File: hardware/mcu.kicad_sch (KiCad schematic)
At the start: 36 parts, among them U1 74LVC125, U2 STM32F407VETx, U3 24LC64, U7 74LVC125, X1 12MHz

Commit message: Update PrntrBoard fabrication files.
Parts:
- X1: Part # (none) -> SIT1602AI-22-33E-12.000000D; Part# SIT1602AI-22-33E-12.000000D -> (none)

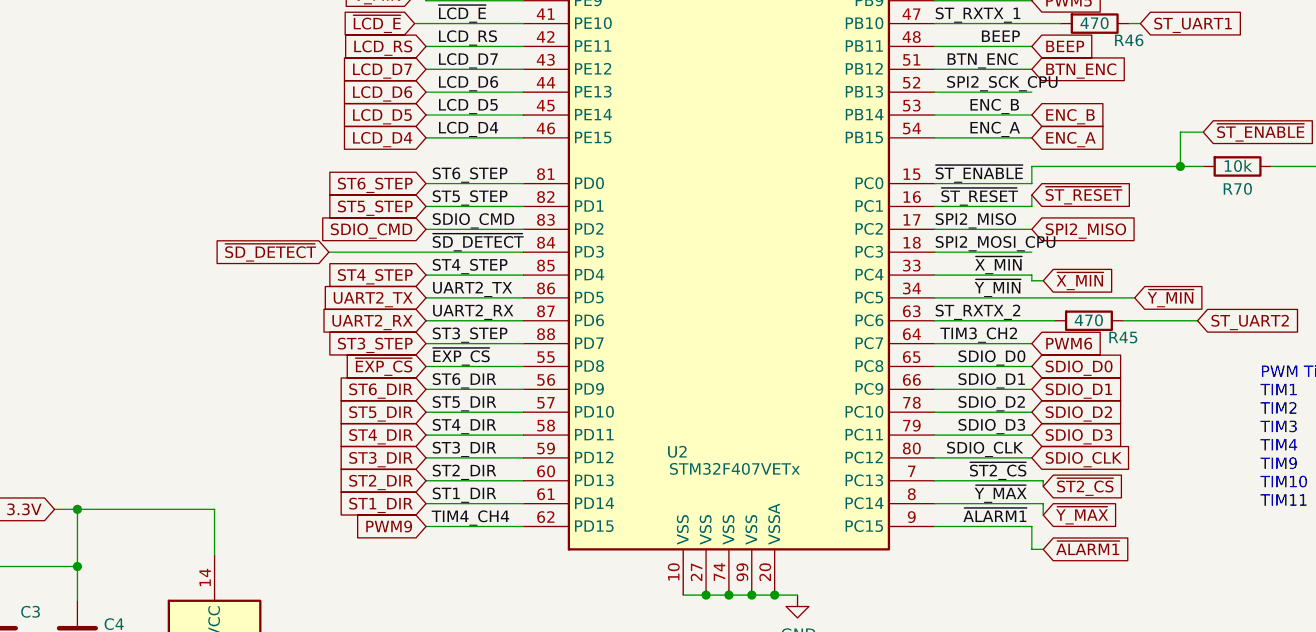
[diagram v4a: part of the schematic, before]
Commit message: Added CAN
- Added CAN interface (PD0-1) with RJ 6p6c terminal
- SD card moved to back /left side and switched to SPI mode
- removed  EXP4 headrr
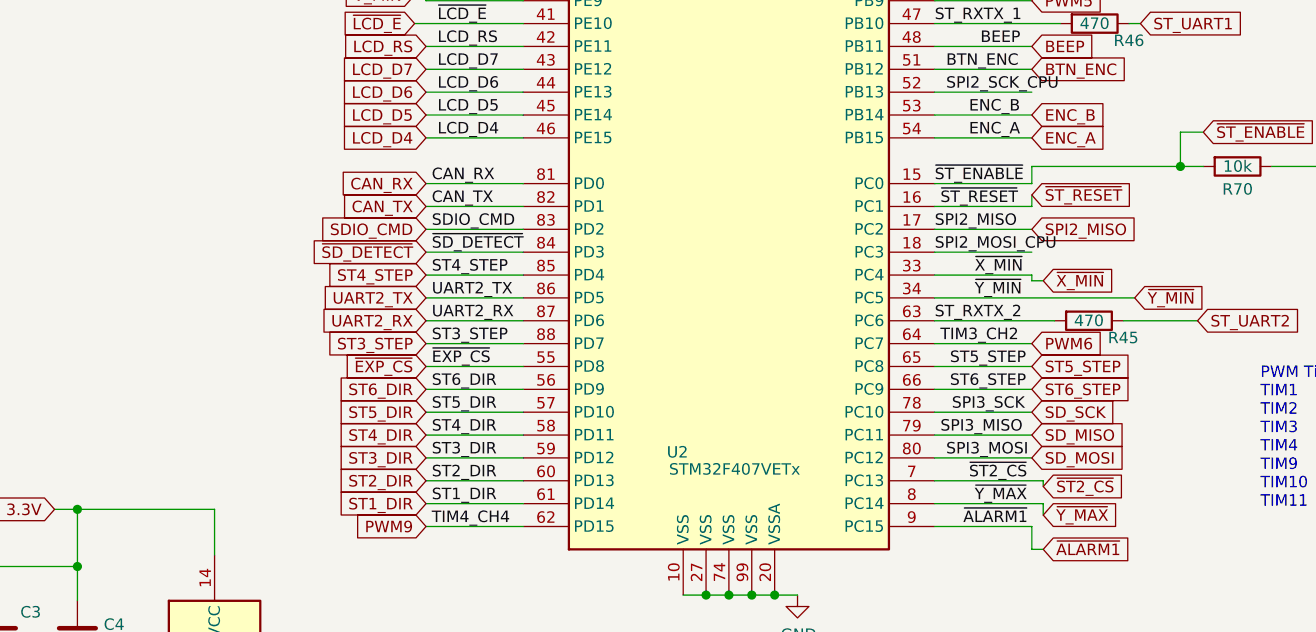
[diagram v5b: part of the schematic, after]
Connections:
- net SDIO_D0 is gone; now on net ST5_STEP: U2.65 (PC8)
- net SDIO_D1 is gone; now on net ST6_STEP: U2.66 (PC9)
- net ST5_STEP: no longer U2.82 (PD1)
- net ST6_STEP: no longer U2.81 (PD0)
- net SDIO_CLK renamed SD_MOSI
- net SDIO_D2 renamed SD_SCK
- net SDIO_D3 renamed SD_MISO
- new net CAN_RX: U2.81 (PD0)
- new net CAN_TX: U2.82 (PD1)
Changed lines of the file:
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@@
   (junction (at 269.24 155.575) (diameter 1.016) (color 0 0 0 0))
   (no_connect (at 262.255 53.975))
+  (no_connect (at 262.255 75.565))
+  (no_connect (at 262.255 64.77))
   (no_connect (at 211.455 89.535))
   (no_connect (at 80.645 69.85))
-  (no_connect (at 262.255 64.77))
-  (no_connect (at 262.255 75.565))
   (wire (pts (xy 22.225 160.655) (xy 31.115 160.655))
     (stroke (width 0) (type solid) (color 0 0 0 0))
@@
     (stroke (width 0) (type solid) (color 0 0 0 0))
   )
-  (wire (pts (xy 59.055 125.73) (xy 80.645 125.73))
-    (stroke (width 0) (type solid) (color 0 0 0 0))
-  )
   (wire (pts (xy 59.69 85.09) (xy 80.645 85.09))
     (stroke (width 0) (type solid) (color 0 0 0 0))
@@
     (stroke (width 0) (type solid) (color 0 0 0 0))
   )
+  (wire (pts (xy 69.85 125.73) (xy 80.645 125.73))
+    (stroke (width 0) (type solid) (color 0 0 0 0))
+  )
   (wire (pts (xy 70.485 177.8) (xy 86.995 177.8))
     (stroke (width 0) (type solid) (color 0 0 0 0))
@@
     (effects (font (size 1.27 1.27)) (justify left bottom))
   )
-  (label "ST6_STEP" (at 70.485 118.11 0)
-    (effects (font (size 1.27 1.27)) (justify left bottom))
-  )
-  (label "ST5_STEP" (at 70.485 120.65 0)
+  (label "CAN_RX" (at 70.485 118.11 0)
+    (effects (font (size 1.27 1.27)) (justify left bottom))
+  )
+  (label "CAN_TX" (at 70.485 120.65 0)
     (effects (font (size 1.27 1.27)) (justify left bottom))
   )
@@
     (effects (font (size 1.27 1.27)) (justify left bottom))
   )
+  (label "SPI3_MISO" (at 127 146.05 0)
+    (effects (font (size 1.27 1.27)) (justify left bottom))
+  )
   (label "SPI2_MOSI_CPU" (at 127 174.625 0)
     (effects (font (size 1.27 1.27)) (justify left bottom))
@@
     (effects (font (size 1.27 1.27)) (justify left bottom))
   )
-  (label "SDIO_CLK" (at 127.635 148.59 0)
+  (label "SPI3_MOSI" (at 127.635 148.59 0)
     (effects (font (size 1.27 1.27)) (justify left bottom))
   )
@@
     (effects (font (size 1.27 1.27)) (justify left bottom))
   )
+  (label "SPI3_SCK" (at 128.27 143.51 0)
+    (effects (font (size 1.27 1.27)) (justify left bottom))
+  )
   (label "USB_D-" (at 128.905 59.69 0)
     (effects (font (size 1.27 1.27)) (justify left bottom))
@@
     (effects (font (size 1.27 1.27)) (justify left bottom))
   )
-  (label "SDIO_D0" (at 128.905 138.43 0)
-    (effects (font (size 1.27 1.27)) (justify left bottom))
-  )
-  (label "SDIO_D1" (at 128.905 140.97 0)
-    (effects (font (size 1.27 1.27)) (justify left bottom))
-  )
-  (label "SDIO_D2" (at 128.905 143.51 0)
-    (effects (font (size 1.27 1.27)) (justify left bottom))
-  )
-  (label "SDIO_D3" (at 128.905 146.05 0)
-    (effects (font (size 1.27 1.27)) (justify left bottom))
-  )
   (label "~ALARM1" (at 129.54 156.21 0)
     (effects (font (size 1.27 1.27)) (justify left bottom))
@@
     (effects (font (size 1.27 1.27)) (justify left bottom))
   )
+  (label "ST5_STEP" (at 136.525 138.43 180)
+    (effects (font (size 1.27 1.27)) (justify right bottom))
+  )
+  (label "ST6_STEP" (at 136.525 140.97 180)
+    (effects (font (size 1.27 1.27)) (justify right bottom))
+  )
   (label "BOOT0" (at 190.5 78.105 0)
     (effects (font (size 1.27 1.27)) (justify left bottom))
@@
     (effects (font (size 1.27 1.27)) (justify right))
   )
-  (global_label "~SD_DETECT" (shape input) (at 59.055 125.73 180)    (property "Intersheet References" "${INTERSHEET_REFS}" (id 0) (at 0 0 0)
-      (effects (font (size 1.27 1.27)) hide)
-    )
-    (effects (font (size 1.27 1.27)) (justify right))
-  )
   (global_label "~ST3_CS" (shape input) (at 59.69 85.09 180)    (property "Intersheet References" "${INTERSHEET_REFS}" (id 0) (at 0 0 0)
       (effects (font (size 1.27 1.27)) hide)
@@
     (effects (font (size 1.27 1.27)) (justify right))
   )
-  (global_label "ST6_STEP" (shape input) (at 69.85 118.11 180)    (property "Intersheet References" "${INTERSHEET_REFS}" (id 0) (at 0 0 0)
-      (effects (font (size 1.27 1.27)) hide)
-    )
-    (effects (font (size 1.27 1.27)) (justify right))
-  )
-  (global_label "ST5_STEP" (shape input) (at 69.85 120.65 180)    (property "Intersheet References" "${INTERSHEET_REFS}" (id 0) (at 0 0 0)
-      (effects (font (size 1.27 1.27)) hide)
+  (global_label "CAN_RX" (shape input) (at 69.85 118.11 180)    (property "Intersheet References" "${INTERSHEET_REFS}" (id 0) (at 57.5067 120.5706 0)
+      (effects (font (size 1.27 1.27)) (justify right) hide)
+    )
+    (effects (font (size 1.27 1.27)) (justify right))
+  )
+  (global_label "CAN_TX" (shape input) (at 69.85 120.65 180)    (property "Intersheet References" "${INTERSHEET_REFS}" (id 0) (at 57.8091 118.0306 0)
+      (effects (font (size 1.27 1.27)) (justify right) hide)
     )
     (effects (font (size 1.27 1.27)) (justify right))
@@
     (effects (font (size 1.27 1.27)) (justify right))
   )
+  (global_label "~SD_DETECT" (shape input) (at 69.85 125.73 180)    (property "Intersheet References" "${INTERSHEET_REFS}" (id 0) (at 10.795 0 0)
+      (effects (font (size 1.27 1.27)) hide)
+    )
+    (effects (font (size 1.27 1.27)) (justify right))
+  )
   (global_label "ST4_STEP" (shape input) (at 69.85 128.27 180)    (property "Intersheet References" "${INTERSHEET_REFS}" (id 0) (at 0 0 0)
       (effects (font (size 1.27 1.27)) hide)
@@
     (effects (font (size 1.27 1.27)) (justify left))
   )
-  (global_label "SDIO_D0" (shape input) (at 137.16 138.43 0)    (property "Intersheet References" "${INTERSHEET_REFS}" (id 0) (at 0 0 0)
-      (effects (font (size 1.27 1.27)) hide)
-    )
-    (effects (font (size 1.27 1.27)) (justify left))
-  )
-  (global_label "SDIO_D1" (shape input) (at 137.16 140.97 0)    (property "Intersheet References" "${INTERSHEET_REFS}" (id 0) (at 0 0 0)
-      (effects (font (size 1.27 1.27)) hide)
-    )
-    (effects (font (size 1.27 1.27)) (justify left))
-  )
-  (global_label "SDIO_D2" (shape input) (at 137.16 143.51 0)    (property "Intersheet References" "${INTERSHEET_REFS}" (id 0) (at 0 0 0)
-      (effects (font (size 1.27 1.27)) hide)
-    )
-    (effects (font (size 1.27 1.27)) (justify left))
-  )
-  (global_label "SDIO_D3" (shape input) (at 137.16 146.05 0)    (property "Intersheet References" "${INTERSHEET_REFS}" (id 0) (at 0 0 0)
-      (effects (font (size 1.27 1.27)) hide)
-    )
-    (effects (font (size 1.27 1.27)) (justify left))
-  )
-  (global_label "SDIO_CLK" (shape input) (at 137.16 148.59 0)    (property "Intersheet References" "${INTERSHEET_REFS}" (id 0) (at 0 0 0)
-      (effects (font (size 1.27 1.27)) hide)
-    )
-    (effects (font (size 1.27 1.27)) (justify left))
+  (global_label "ST5_STEP" (shape input) (at 137.16 138.43 0)    (property "Intersheet References" "${INTERSHEET_REFS}" (id 0) (at 207.01 259.08 0)
+      (effects (font (size 1.27 1.27)) hide)
+    )
+    (effects (font (size 1.27 1.27)) (justify left))
+  )
+  (global_label "ST6_STEP" (shape input) (at 137.16 140.97 0)    (property "Intersheet References" "${INTERSHEET_REFS}" (id 0) (at 207.01 259.08 0)
+      (effects (font (size 1.27 1.27)) hide)
+    )
+    (effects (font (size 1.27 1.27)) (justify left))
+  )
+  (global_label "SD_SCK" (shape input) (at 137.16 143.51 0)    (property "Intersheet References" "${INTERSHEET_REFS}" (id 0) (at 148.2938 143.4306 0)
+      (effects (font (size 1.27 1.27)) (justify left) hide)
+    )
+    (effects (font (size 1.27 1.27)) (justify left))
+  )
+  (global_label "SD_MISO" (shape input) (at 137.16 146.05 0)    (property "Intersheet References" "${INTERSHEET_REFS}" (id 0) (at 149.1404 145.9706 0)
+      (effects (font (size 1.27 1.27)) (justify left) hide)
+    )
+    (effects (font (size 1.27 1.27)) (justify left))
+  )
+  (global_label "SD_MOSI" (shape input) (at 137.16 148.59 0)    (property "Intersheet References" "${INTERSHEET_REFS}" (id 0) (at 149.1404 148.5106 0)
+      (effects (font (size 1.27 1.27)) (justify left) hide)
+    )
+    (effects (font (size 1.27 1.27)) (justify left))
